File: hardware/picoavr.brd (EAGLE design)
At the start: 37.2 x 20.3 mm, 26 parts, among them IC1 MCP1703CB, Q2 12mhz, SW1 SPST_TACT-KMR2, U3 ATMEGA328P, X1 Micro USB

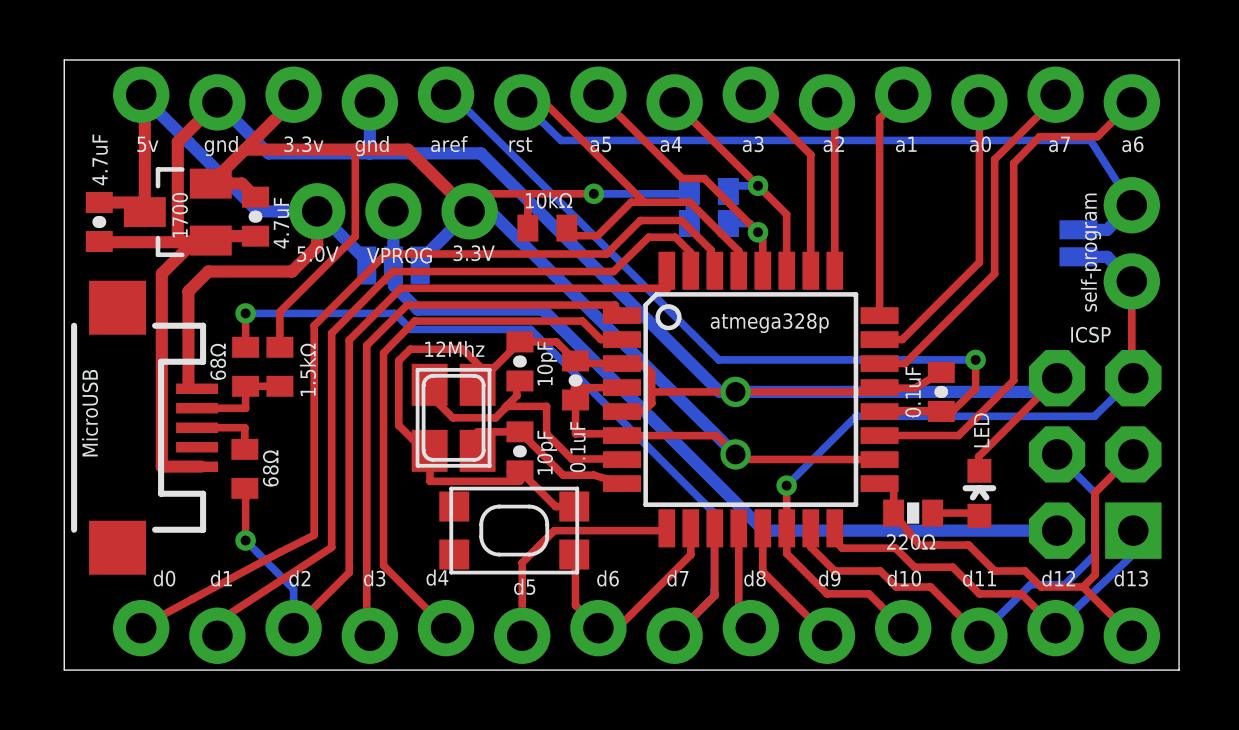
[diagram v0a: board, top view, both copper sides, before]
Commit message: changed button placement
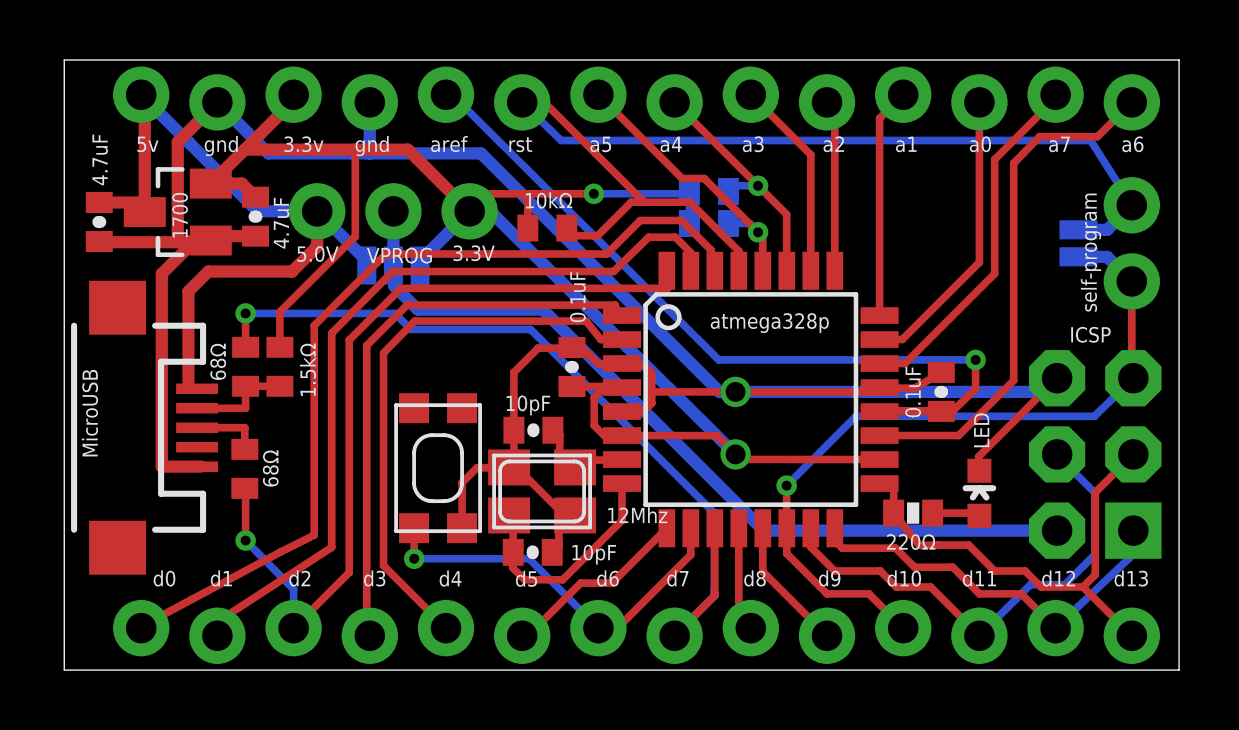
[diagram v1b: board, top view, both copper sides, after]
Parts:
- moved Q2 3.84 mm to (15.9, 5.95), turned to 180 degrees
- moved C4 3.39 mm to (15.6, 3.92), turned to 0 degrees
- moved SW1 3.28 mm to (12.4, 6.73), turned to 270 degrees
- moved C3 2.34 mm to (15.6, 7.99), turned to 180 degrees
- moved C5 0.47 mm to (16.9, 10.1)
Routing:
- net N$6: track 9.71 -> 3.46 mm
- net D6: track 7.76 -> 13.1 mm, vias 0 -> 1
- net GND: track 92.6 -> 88.6 mm
- net N$5: track 6.08 -> 7.67 mm
- net D5: track 7.75 -> 6.30 mm
- net VCC: track 60.8 -> 60.2 mm

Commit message: change led placement
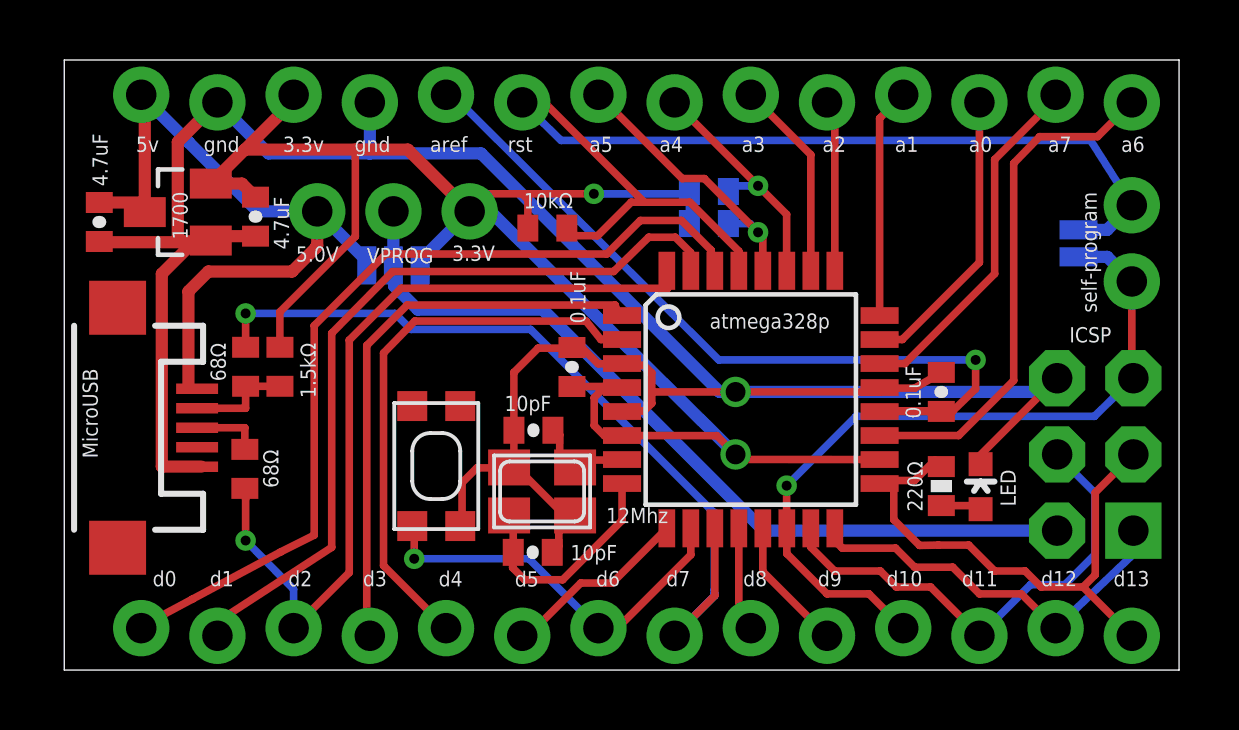
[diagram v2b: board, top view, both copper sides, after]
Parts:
- moved R9 1.30 mm to (29.2, 6.13), turned to 270 degrees
- moved LED2 0.22 mm to (30.5, 6.11)
- moved SW1 0.09 mm to (12.4, 6.80)
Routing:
- net SCK: track 16.4 -> 18.4 mm
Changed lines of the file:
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@@
 <text x="17.3482" y="11.5532" size="0.508" layer="121" font="vector" ratio="12" rot="R90">0.1uF</text>
 <text x="28.5242" y="8.382" size="0.508" layer="121" font="vector" ratio="12" rot="R90">0.1uF</text>
-<text x="27.3558" y="4.0132" size="0.508" layer="121" font="vector" ratio="12">220Ω</text>
-<text x="30.8102" y="7.366" size="0.508" layer="121" font="vector" ratio="12" rot="R90">LED</text>
+<text x="28.5858" y="5.2832" size="0.508" layer="121" font="vector" ratio="12" rot="R90">220Ω</text>
+<text x="31.6902" y="5.456" size="0.508" layer="121" font="vector" ratio="12" rot="R90">LED</text>
 <text x="8.3566" y="9.0678" size="0.508" layer="121" font="vector" ratio="12" rot="R90">1.5kΩ</text>
 <text x="12.9032" y="13.6398" size="0.508" layer="121" font="vector" ratio="12">3.3V</text>
@@
 <element name="JP3" library="SparkFun-Connectors" package="1X14_LOCK" value="M14LOCK" x="2.54" y="19.05" smashed="yes"/>
 <element name="C5" library="SparkFun-Capacitors" package="0402-CAP" value="0.1uF" x="16.898" y="10.102" smashed="yes" rot="R90"/>
-<element name="LED2" library="SparkFun" package="LED-0603" value="GREEN" x="30.48" y="5.8928" smashed="yes"/>
-<element name="R9" library="SparkFun" package="0402-RES" value="220" x="28.2702" y="5.2324" smashed="yes"/>
+<element name="LED2" library="SparkFun" package="LED-0603" value="GREEN" x="30.52" y="6.1128" smashed="yes"/>
+<element name="R9" library="SparkFun" package="0402-RES" value="220" x="29.2102" y="6.1324" smashed="yes" rot="R270"/>
 <element name="C6" library="SparkFun-Capacitors" package="0402-CAP" value="0.1uF" x="29.21" y="9.271" smashed="yes" rot="R90"/>
 <element name="R7" library="resistor" package="R0402" value="1.5k" x="7.1628" y="10.1092" smashed="yes" rot="R90"/>
@@
 </element>
 <element name="SJ2" library="SparkFun-Passives" package="SJ_2S-NO" value="SOLDERJUMPERNO" x="33.782" y="14.224" smashed="yes" rot="MR270"/>
-<element name="SW1" library="adafruit" package="KMR2" value="SPST_TACT-KMR2" x="12.435" y="6.73" rot="R270"/>
+<element name="SW1" library="adafruit" package="KMR2" value="SPST_TACT-KMR2" x="12.375" y="6.8" rot="R270"/>
 </elements>
 <signals>
@@
 <wire x1="19.304" y1="8.636" x2="19.558" y2="8.89" width="0.254" layer="1"/>
 <wire x1="19.558" y1="8.89" x2="19.558" y2="9.271" width="0.254" layer="1"/>
-<wire x1="30.48" y1="6.6428" x2="30.4546" y2="6.6428" width="0.254" layer="1"/>
+<wire x1="30.52" y1="6.8628" x2="30.4546" y2="6.6428" width="0.254" layer="1"/>
 <wire x1="30.4546" y1="6.6428" x2="30.4546" y2="7.112" width="0.254" layer="1"/>
 <wire x1="1.21710625" y1="14.10949375" x2="1.143" y2="14.2852" width="0.254" layer="1"/>
@@
 <wire x1="15.77" y1="10.73" x2="16.876" y2="10.73" width="0.254" layer="1"/>
 <wire x1="16.876" y1="10.73" x2="16.898" y2="10.752" width="0.254" layer="1"/>
-<wire x1="13.235" y1="4.73" x2="13.235" y2="6.245" width="0.254" layer="1"/>
 <wire x1="13.235" y1="6.245" x2="13.73" y2="6.74" width="0.254" layer="1"/>
 <wire x1="13.73" y1="6.74" x2="14.7886" y2="6.74" width="0.254" layer="1"/>
 <wire x1="14.7886" y1="6.74" x2="14.8026" y2="6.754" width="0.254" layer="1"/>
+<wire x1="13.175" y1="4.8" x2="13.235" y2="4.8" width="0.254" layer="1"/>
+<wire x1="13.235" y1="4.8" x2="13.235" y2="6.245" width="0.254" layer="1"/>
 </signal>
 <signal name="VCC">
@@
 <contactref element="R9" pad="1"/>
 <wire x1="27.1526" y1="6.217" x2="27.6262" y2="6.3186" width="0.254" layer="1"/>
-<wire x1="27.6262" y1="6.3186" x2="27.6202" y2="5.2324" width="0.254" layer="1"/>
-<wire x1="27.6202" y1="5.2324" x2="28.4838" y2="4.1552" width="0.254" layer="1"/>
 <wire x1="28.4838" y1="4.1552" x2="29.1084" y2="4.1656" width="0.254" layer="1"/>
 <wire x1="29.1084" y1="4.1656" x2="30.1244" y2="4.1656" width="0.254" layer="1"/>
@@
 <wire x1="33.9344" y1="2.7686" x2="34.3408" y2="3.175" width="0.254" layer="1"/>
 <wire x1="34.3408" y1="3.175" x2="34.3408" y2="5.9182" width="0.254" layer="1"/>
+<wire x1="27.6262" y1="6.3186" x2="27.6262" y2="5.0128" width="0.254" layer="1"/>
+<wire x1="27.6262" y1="5.0128" x2="28.4838" y2="4.1552" width="0.254" layer="1"/>
+<wire x1="27.6262" y1="6.3186" x2="28.3186" y2="6.3186" width="0.254" layer="1"/>
+<wire x1="28.3186" y1="6.3186" x2="29" y2="7" width="0.254" layer="1"/>
+<wire x1="29" y1="7" x2="29" y2="6.9926" width="0.254" layer="1"/>
+<wire x1="29" y1="6.9926" x2="29.2102" y2="6.7824" width="0.254" layer="1"/>
 </signal>
 <signal name="D0">
@@
 <wire x1="18.415" y1="1.397" x2="17.78" y2="1.397" width="0.254" layer="1"/>
 <contactref element="SW1" pad="2"/>
-<wire x1="11.635" y1="4.73" x2="11.635" y2="3.965" width="0.254" layer="1"/>
-<wire x1="11.635" y1="3.965" x2="11.64" y2="3.71" width="0.254" layer="1"/>
 <via x="11.64" y="3.71" extent="1-16" drill="0.3302"/>
 <wire x1="11.64" y1="3.71" x2="15.467" y2="3.71" width="0.254" layer="16"/>
 <wire x1="15.467" y1="3.71" x2="17.78" y2="1.397" width="0.254" layer="16"/>
+<wire x1="11.575" y1="4.8" x2="11.64" y2="4.8" width="0.254" layer="1"/>
+<wire x1="11.64" y1="4.8" x2="11.64" y2="3.71" width="0.254" layer="1"/>
 </signal>
 <signal name="B0">
@@
 <contactref element="LED2" pad="A"/>
 <contactref element="R9" pad="2"/>
-<wire x1="28.9202" y1="5.2324" x2="30.48" y2="5.2324" width="0.254" layer="1"/>
-<wire x1="30.48" y1="5.2324" x2="30.48" y2="5.1428" width="0.254" layer="1"/>
+<wire x1="30.48" y1="5.2324" x2="30.52" y2="5.3628" width="0.254" layer="1"/>
+<wire x1="29.2102" y1="5.4824" x2="30.52" y2="5.4824" width="0.254" layer="1"/>
+<wire x1="30.52" y1="5.4824" x2="30.52" y2="5.3628" width="0.254" layer="1"/>
 </signal>
 <signal name="AREF">

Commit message: new hardware revision
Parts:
- removed LED2: GREEN, SparkFun:LED-0603
- removed POWER: (no value), SparkFun-Connectors:1X03_NO_SILK
- removed R9: 220, SparkFun:0402-RES
- added LED: GREEN, SparkFun:LED-0603
- added R4: 10k, resistor:R0402
- R1, R2: value 4.7k -> 68; device SparkFun:0402-RES -> resistor:R0402
- R3: value 68 -> 1.5k
- R5: value 68 -> 220; device resistor:R0402 -> SparkFun:0402-RES
- R6: value 10k -> 4.7k; device resistor:R0402 -> SparkFun:0402-RES
- R7: value 1.5k -> 4.7k; device resistor:R0402 -> SparkFun:0402-RES
- moved R5 22.5 mm to (28.5, 5.71)
- moved R1 18.4 mm to (5.66, 6.60), flipped to the top, turned to 270 degrees
- moved R2 16.5 mm to (5.68, 10.0), flipped to the top, turned to 90 degrees
- moved R7 14.0 mm to (20.4, 14.7), flipped to the bottom, turned to 180 degrees
- moved R6 4.54 mm to (20.4, 13.4), flipped to the bottom, turned to 180 degrees
- moved SELF_PROGRAM 3.79 mm to (32.4, 13.4), turned to 0 degrees
- moved IC1 2.24 mm to (5.54, 13.9)
- moved C5 2.18 mm to (14.9, 9.16), turned to 180 degrees
- moved C2 2.14 mm to (8.35, 14.4)
- moved JP3 2.12 mm to (1.84, 17.1)
- moved R3 2.01 mm to (6.83, 8.27)
- moved SJ1 1.98 mm to (8.99, 13.2), turned to 90 degrees
- moved C1 1.69 mm to (2.74, 14.4), turned to 90 degrees
- moved C6 0.83 mm to (28.5, 8.85)
- moved U3 0.83 mm to (22.1, 8.60)
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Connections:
- net GND: now also LED.C; no longer LED2.C
- net N$11: now also LED.A, R5.2; no longer LED2.A, R9.2
- net N$2: now also R1.1; no longer R5.1
- net N$4: now also R2.1; no longer R7.1
- net RESET: now also R4.2; no longer R6.2
- net SCK: now also R5.1; no longer R9.1
- net SCL: now also R7.2; no longer R2.2
- net SDA: now also R6.2; no longer R1.2
- net USB_DMINUS: now also R2.2; no longer R3.2
- net USB_DPLUS: now also R1.2; no longer R5.2
- net USB_VBUS: no longer POWER.1
- net VCC: now also R3.2, R4.1, R7.1; no longer POWER.3, R1.1, R2.1, R7.2
- net VPROG: no longer POWER.2
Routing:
- net USB_VBUS: track 25.7 -> 15.9 mm, vias 0 -> 1
- net RESET: track 38.0 -> 33.1 mm
- net GND: track 88.8 -> 93.0 mm, vias 1 -> 2
- net USB_DPLUS: track 28.4 -> 26.6 mm
- net A6: track 17.3 -> 15.5 mm
- net A2: track 5.87 -> 4.13 mm
- net USB_DMINUS: track 28.5 -> 26.8 mm
- net A3: track 6.70 -> 5.11 mm
- net A0: track 9.73 -> 8.16 mm
- net A7: track 11.8 -> 10.3 mm
- net ISP_RESET: track 25.6 -> 26.9 mm
- net D4: track 18.7 -> 17.4 mm
- net D3: track 19.3 -> 18.1 mm
- net D0: track 29.3 -> 28.3 mm
- net VPROG: track 28.0 -> 26.9 mm
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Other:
- board size 37.2 x 20.3 mm -> 36.4 x 18.3 mm
- board text added: "C1"
- board text added: "C2"
- board text added: "C3"
- board text added: "C4"
- board text added: "C5"
- board text added: "C6"
- board text added: "IC1"
- board text added: "PicoAVR rev 1.3"
- board text added: "Q1"
- board text added: "R1"
- board text added: "R2"
- board text added: "R3"
- board text added: "R4"
- board text added: "R5"
- board text added: "SW1"
- board text added: "U1"
- board text removed: "0.1uF"
- board text removed: "1.5kΩ"
- board text removed: "10kΩ"
- board text removed: "10pF"
- board text removed: "12Mhz"
- board text removed: "1700"
- board text removed: "220Ω"
- board text removed: "3.3V"
- board text removed: "4.7kΩ (SCL)"
- board text removed: "4.7kΩ (SDA)"
- board text removed: "4.7uF"
- board text removed: "5.0V"
- board text removed: "68Ω"
- board text removed: "PicoAVR rev 1.2"
- board text removed: "VPROG"
- board text removed: "atmega328p"

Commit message: moved labels
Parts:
- moved R6 0.21 mm to (20.3, 13.2)
- moved R7 0.21 mm to (20.3, 14.5)
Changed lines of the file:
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@@
 <text x="7.77748125" y="8.2905625" size="0.508" layer="121" font="vector" ratio="12" rot="R90" align="center">R3</text>
 <text x="14.91995625" y="14.5288" size="0.508" layer="121" font="vector" ratio="12" rot="R90" align="center">R4</text>
-<text x="30.2006" y="11.689078125" size="1.016" layer="122" font="vector" ratio="12" rot="MR0">PicoAVR rev 1.3</text>
+<text x="29.804359375" y="11.2928375" size="1.016" layer="122" font="vector" ratio="12" rot="MR0">PicoAVR rev 1.3</text>
 <text x="1.275075" y="15.304521875" size="0.508" layer="121" font="vector" ratio="12">5v</text>
 <text x="3.423915625" y="15.304521875" size="0.508" layer="121" font="vector" ratio="12">gnd</text>
@@
 <text x="27.863796875" y="15.3197625" size="0.508" layer="122" font="vector" ratio="12" rot="MR0">pc1</text>
 <text x="30.403796875" y="15.311121875" size="0.508" layer="122" font="vector" ratio="12" rot="MR0">pc0</text>
-<text x="32.867596875" y="15.3197625" size="0.508" layer="122" font="vector" ratio="12" rot="MR0">pc7</text>
-<text x="35.458396875" y="15.3197625" size="0.508" layer="122" font="vector" ratio="12" rot="MR0">pc6</text>
+<text x="32.440878125" y="15.3197625" size="0.508" layer="122" font="vector" ratio="12" rot="MR0">pc7</text>
+<text x="36.1848375" y="15.335003125" size="0.508" layer="122" font="vector" ratio="12" rot="MR0">pc6</text>
 <text x="3.048" y="2.794" size="0.508" layer="122" font="vector" ratio="12" rot="MR0">pd0</text>
 <text x="5.588" y="2.794" size="0.508" layer="122" font="vector" ratio="12" rot="MR0">pd1</text>
@@
 <attribute name="VALUE" x="31.1267375" y="10.232759375" size="1.27" layer="27"/>
 </element>
-<element name="R6" library="SparkFun" package="0402-RES" value="4.7k" x="20.4216" y="13.426340625" smashed="yes" rot="MR180"/>
-<element name="R7" library="SparkFun" package="0402-RES" value="4.7k" x="20.4216" y="14.694440625" smashed="yes" rot="MR180"/>
+<element name="R6" library="SparkFun" package="0402-RES" value="4.7k" x="20.335240625" y="13.23838125" smashed="yes" rot="MR180"/>
+<element name="R7" library="SparkFun" package="0402-RES" value="4.7k" x="20.335240625" y="14.50648125" smashed="yes" rot="MR180"/>
 <element name="SJ1" library="SparkFun-Passives" package="SJ_3" value="" x="8.9916" y="13.1572" smashed="yes" rot="MR90">
 <attribute name="VALUE" x="8.9916" y="13.0571" size="0.02" layer="28" rot="MR90"/>
@@
 <contactref element="R7" pad="1"/>
 <contactref element="SJ1" pad="3"/>
-<wire x1="19.7716" y1="13.426340625" x2="19.7716" y2="14.694440625" width="0.254" layer="16"/>
+<wire x1="19.685240625" y1="13.23838125" x2="19.685240625" y2="14.50648125" width="0.254" layer="16"/>
 <via x="21.6662" y="6.8952" extent="1-16" drill="0.6604"/>
 <wire x1="17.8489" y1="8.997" x2="17.2585" y2="8.997" width="0.254" layer="1"/>
@@
 <wire x1="26.4341" y1="6.597" x2="21.9825" y2="6.597" width="0.254" layer="1"/>
 <wire x1="21.9825" y1="6.597" x2="21.6662" y2="6.8952" width="0.254" layer="1"/>
-<wire x1="19.7716" y1="14.694440625" x2="17.884678125" y2="14.694440625" width="0.254" layer="16"/>
-<wire x1="17.884678125" y1="14.694440625" x2="17.49551875" y2="14.5288" width="0.254" layer="16"/>
+<wire x1="19.685240625" y1="14.50648125" x2="17.5748" y2="14.516640625" width="0.254" layer="16"/>
+<wire x1="17.5748" y1="14.516640625" x2="17.49551875" y2="14.5288" width="0.254" layer="16"/>
 <via x="17.49551875" y="14.5288" extent="1-16" drill="0.3302"/>
 <wire x1="11.083821875" y1="14.4272" x2="11.048990625" y2="14.39236875" width="0.254" layer="1"/>
@@
 <wire x1="22.265640625" y1="15.814040625" x2="21.605240625" y2="15.814040625" width="0.254" layer="1"/>
 <wire x1="21.605240625" y1="15.814040625" x2="20.447" y2="16.97228125" width="0.254" layer="1"/>
-<wire x1="22.067421875" y1="13.426340625" x2="23.342596875" y2="14.5288" width="0.254" layer="16"/>
+<wire x1="21.777859375" y1="13.223140625" x2="23.342596875" y2="14.5288" width="0.254" layer="16"/>
 <via x="23.342596875" y="14.5288" extent="1-16" drill="0.3302"/>
 <wire x1="23.342596875" y1="14.5288" x2="23.31211875" y2="14.7088" width="0.254" layer="1"/>
 <wire x1="23.31211875" y1="14.7088" x2="23.3415" y2="14.73818125" width="0.254" layer="1"/>
-<wire x1="21.0716" y1="13.426340625" x2="22.067421875" y2="13.426340625" width="0.254" layer="16"/>
+<wire x1="20.985240625" y1="13.23838125" x2="21.777859375" y2="13.223140625" width="0.254" layer="16"/>
 <wire x1="20.447" y1="16.97228125" x2="19.6215" y2="16.923" width="0" layer="19" extent="1-1"/>
 </signal>
@@
 <wire x1="21.300440625" y1="15.458440625" x2="18.800059375" y2="15.458440625" width="0.254" layer="1"/>
 <wire x1="18.800059375" y1="15.458440625" x2="17.0815" y2="17.177" width="0.254" layer="1"/>
-<wire x1="21.0716" y1="14.694440625" x2="21.900421875" y2="14.694440625" width="0.254" layer="16"/>
-<wire x1="21.900421875" y1="14.694440625" x2="22.19579375" y2="14.5288" width="0.254" layer="16"/>
+<wire x1="20.985240625" y1="14.50648125" x2="22.174740625" y2="14.50648125" width="0.254" layer="16"/>
+<wire x1="22.174740625" y1="14.50648125" x2="22.19579375" y2="14.5288" width="0.254" layer="16"/>
 <via x="22.19579375" y="14.5288" extent="1-16" drill="0.3302"/>
 <wire x1="22.19579375" y1="14.5288" x2="21.879440625" y2="14.879440625" width="0.254" layer="1"/>
